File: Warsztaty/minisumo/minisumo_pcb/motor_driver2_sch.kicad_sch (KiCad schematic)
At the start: 6 parts, among them U2 TB6612FNG

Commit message: chyba gotowy schemat
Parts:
- removed C3, C6: 10nF, Capacitor_SMD:C_0805_2012Metric_Pad1.18x1.45mm_HandSolder, symbol Device:C_Small
- removed C4, C5: 10uF, Capacitor_Tantalum_SMD:CP_EIA-3528-12_Kemet-T, symbol Device:C_Polarized_Small
- removed M1: ~, Motors_KoNaR:KoNaR_Motor, symbol Motors_KoNaR:Motor
- removed U2: TB6612FNG, Package_SO:SSOP-24_5.3x8.2mm_P0.65mm, symbol Driver_Motor:TB6612FNG
- added C27, C30: 10uF, Capacitor_SMD:C_0805_2012Metric_Pad1.18x1.45mm_HandSolder, symbol Device:C_Polarized_Small
- added C28, C29: 10nF, Capacitor_SMD:C_0805_2012Metric_Pad1.18x1.45mm_HandSolder, symbol Device:C_Small
- added M2: ~, Motors_KoNaR:KoNaR_Motor, symbol Motors_KoNaR:Motor
- added U14: TB6612FNG, Package_SO:SSOP-24_5.3x8.2mm_P0.65mm, symbol Driver_Motor:TB6612FNG
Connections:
- net +5V: now also C27.1, C28.1, U14.19 (STBY), U14.20 (VCC)
- net +BATT: now also C29.1, C30.1, U14.13 (VM2), U14.14 (VM3), U14.24 (VM1)
- net GND: now also C27.2, C28.2, C29.2, C30.2, U14.10 (PGND2), U14.18 (GND), U14.3 (PGND1), U14.4 (PGND1), U14.9 (PGND2)
- new net: M2.1, U14.5 (AO2), U14.6 (AO2), U14.7 (BO2), U14.8 (BO2)
- new net: M2.2, U14.1 (AO1), U14.11 (BO1), U14.12 (BO1), U14.2 (AO1)
- new net DIRA_2: U14.17 (BIN1), U14.21 (AIN1)
- new net DIRB_2: U14.16 (BIN2), U14.22 (AIN2)
- new net PWM2: U14.15 (PWMB), U14.23 (PWMA)
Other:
- note added: "Motor 2 driver"
- note removed: "Motor 1 driver"

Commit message: stan przed usunięciem jednego czujnika lini
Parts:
- C27, C30: footprint Capacitor_SMD:C_0805_2012Metric_Pad1.18x1.45mm_HandSolder -> Capacitor_Tantalum_SMD:CP_EIA-3528-12_Kemet-T
- C28, C29: footprint Capacitor_SMD:C_0805_2012Metric_Pad1.18x1.45mm_HandSolder -> Capacitor_SMD:C_0805_2012Metric
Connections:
- net MOTOR_IN2: now reaches M2.1, U14.5 (AO2), U14.6 (AO2), U14.7 (BO2), U14.8 (BO2)
- net MOTOR_IN1: now reaches M2.2, U14.1 (AO1), U14.11 (BO1), U14.12 (BO1), U14.2 (AO1)
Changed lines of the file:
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@@
+		)
+	)
+	(label "MOTOR_IN2"
+		(at 76.2 55.88 0)
+		(fields_autoplaced yes)
+		(effects
+			(font
+				(size 1.27 1.27)
+			)
+			(justify left bottom)
+		)
+	)
+	(label "MOTOR_IN1"
+		(at 76.2 45.72 0)
+		(fields_autoplaced yes)
+		(effects
+			(font
+				(size 1.27 1.27)
+			)
+			(justify left bottom)
 		)
 	)
@@
 			)
 		)
-		(property "Footprint" "Capacitor_SMD:C_0805_2012Metric_Pad1.18x1.45mm_HandSolder"
+		(property "Footprint" "Capacitor_SMD:C_0805_2012Metric"
 			(at 72.39 29.21 0)
 			(effects
@@
 			)
 		)
-		(property "Footprint" "Capacitor_SMD:C_0805_2012Metric_Pad1.18x1.45mm_HandSolder"
+		(property "Footprint" "Capacitor_Tantalum_SMD:CP_EIA-3528-12_Kemet-T"
 			(at 77.47 29.21 0)
 			(effects
@@
 			)
 		)
-		(property "Footprint" "Capacitor_SMD:C_0805_2012Metric_Pad1.18x1.45mm_HandSolder"
+		(property "Footprint" "Capacitor_SMD:C_0805_2012Metric"
 			(at 31.75 30.48 0)
 			(effects
@@
 			)
 		)
-		(property "Footprint" "Capacitor_SMD:C_0805_2012Metric_Pad1.18x1.45mm_HandSolder"
+		(property "Footprint" "Capacitor_Tantalum_SMD:CP_EIA-3528-12_Kemet-T"
 			(at 26.67 30.48 0)
 			(effects

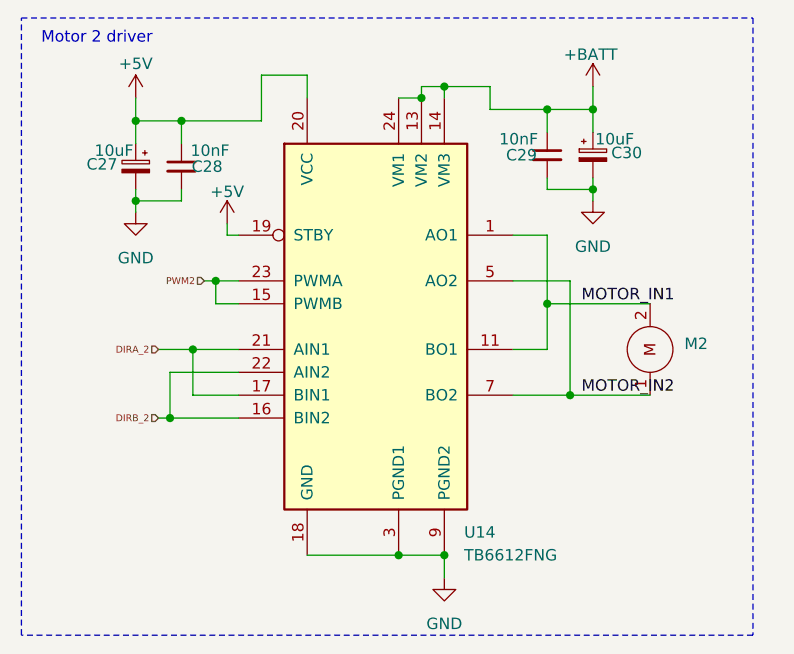
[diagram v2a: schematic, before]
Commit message: Wstępny wyglad robota i płytki
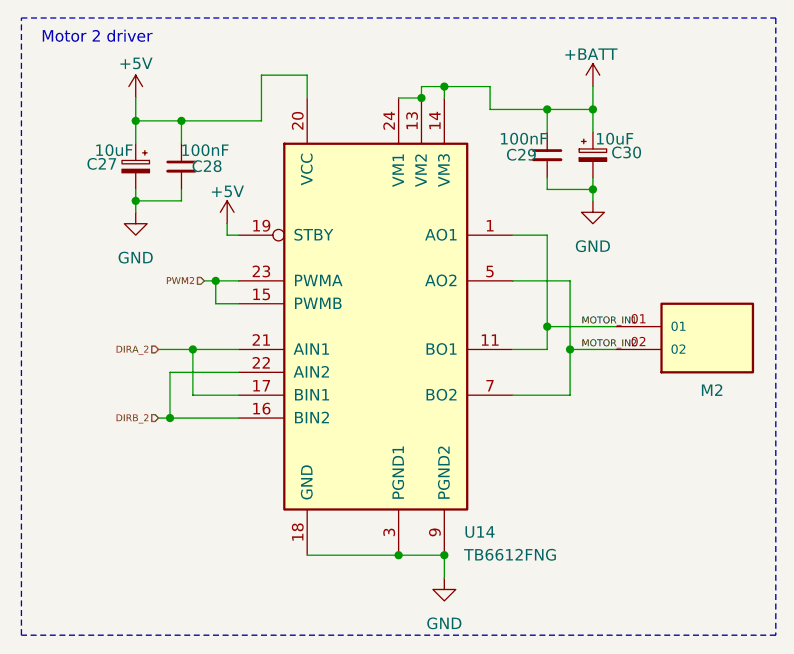
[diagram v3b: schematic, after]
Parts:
- removed M2: ~, Motors_KoNaR:KoNaR_Motor, symbol Motors_KoNaR:Motor
- added M2: HTSW-102-08-L-S, HTSW-102-08-L-S:SAMTEC_HTSW-102-08-L-S, symbol HTSW-102-08-L-S:HTSW-102-08-L-S
- C28, C29: value 10nF -> 100nF
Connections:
- net MOTOR_IN1: now also M2.01
- net MOTOR_IN2: now also M2.02
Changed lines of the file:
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@@
+	)
+	(junction
+		(at 74.93 50.8)
+		(diameter 0)
+		(color 0 0 0 0)
+	)
+	(junction
+		(at 72.39 48.26)
+		(diameter 0)
+		(color 0 0 0 0)
 	)
 	(junction
@@
 	)
 	(junction
-		(at 74.93 55.88)
-		(diameter 0)
-		(color 0 0 0 0)
-	)
-	(junction
 		(at 26.67 34.29)
-		(diameter 0)
-		(color 0 0 0 0)
-	)
-	(junction
-		(at 72.39 45.72)
 		(diameter 0)
 		(color 0 0 0 0)
@@
 	(wire
 		(pts
+			(xy 74.93 50.8) (xy 74.93 55.88)
+		)
+		(stroke
+			(width 0)
+			(type default)
+		)
+	)
+	(wire
+		(pts
 			(xy 31.75 25.4) (xy 40.64 25.4)
 		)
@@
 	(wire
 		(pts
-			(xy 72.39 45.72) (xy 72.39 50.8)
-		)
-		(stroke
-			(width 0)
-			(type default)
-		)
-	)
-	(wire
-		(pts
 			(xy 34.29 43.18) (xy 35.56 43.18)
 		)
@@
 	(wire
 		(pts
-			(xy 72.39 38.1) (xy 72.39 45.72)
-		)
-		(stroke
-			(width 0)
-			(type default)
-		)
-	)
-	(wire
-		(pts
-			(xy 74.93 55.88) (xy 83.82 55.88)
+			(xy 72.39 38.1) (xy 72.39 48.26)
 		)
 		(stroke
@@
 	(wire
 		(pts
+			(xy 72.39 48.26) (xy 80.01 48.26)
+		)
+		(stroke
+			(width 0)
+			(type default)
+		)
+	)
+	(wire
+		(pts
 			(xy 30.48 58.42) (xy 38.1 58.42)
 		)
@@
 	(wire
 		(pts
-			(xy 74.93 43.18) (xy 74.93 55.88)
+			(xy 74.93 43.18) (xy 74.93 50.8)
 		)
 		(stroke
@@
 	(wire
 		(pts
+			(xy 72.39 48.26) (xy 72.39 50.8)
+		)
+		(stroke
+			(width 0)
+			(type default)
+		)
+	)
+	(wire
+		(pts
 			(xy 40.64 20.32) (xy 40.64 25.4)
 		)
@@
 	(wire
 		(pts
+			(xy 74.93 50.8) (xy 80.01 50.8)
+		)
+		(stroke
+			(width 0)
+			(type default)
+		)
+	)
+	(wire
+		(pts
 			(xy 36.83 36.83) (xy 36.83 38.1)
 		)
@@
 		(pts
 			(xy 66.04 24.13) (xy 66.04 21.59)
-		)
-		(stroke
-			(width 0)
-			(type default)
-		)
-	)
-	(wire
-		(pts
-			(xy 72.39 45.72) (xy 83.82 45.72)
 		)
 		(stroke
@@
 	(rectangle
 		(start 13.97 13.97)
-		(end 95.25 82.55)
+		(end 97.79 82.55)
 		(stroke
 			(width 0)
@@
 	)
 	(label "MOTOR_IN2"
-		(at 76.2 55.88 0)
+		(at 76.2 50.8 0)
 		(fields_autoplaced yes)
 		(effects
 			(font
-				(size 1.27 1.27)
+				(size 0.762 0.762)
 			)
 			(justify left bottom)
@@
 	)
 	(label "MOTOR_IN1"
-		(at 76.2 45.72 0)
+		(at 76.2 48.26 0)
 		(fields_autoplaced yes)
 		(effects
 			(font
-				(size 1.27 1.27)
+				(size 0.762 0.762)
 			)
 			(justify left bottom)
@@
 			)
 		)
-		(property "Value" "10nF"
+		(property "Value" "100nF"
 			(at 67.056 27.432 0)
 			(effects
@@
 	)
 	(symbol
+		(lib_id "HTSW-102-08-L-S:HTSW-102-08-L-S")
+		(at 90.17 48.26 0)
+		(unit 1)
+		(exclude_from_sim no)
+		(in_bom yes)
+		(on_board yes)
+		(dnp no)
+		(property "Reference" "M2"
+			(at 89.408 55.372 0)
+			(effects
+				(font
+					(size 1.27 1.27)
+				)
+				(justify left)
+			)
+		)
+		(property "Value" "HTSW-102-08-L-S"
+			(at 76.962 43.434 0)
+			(effects
+				(font
+					(size 1.27 1.27)
+				)
+				(justify left)
+				(hide yes)
+			)
+		)
+		(property "Footprint" "HTSW-102-08-L-S:SAMTEC_HTSW-102-08-L-S"
+			(at 90.17 48.26 0)
+			(effects
+				(font
+					(size 1.27 1.27)
+				)
+				(justify bottom)
+				(hide yes)
+			)
+		)
+		(property "Datasheet" ""
+			(at 90.17 48.26 0)
+			(effects
+				(font
+					(size 1.27 1.27)
+				)
+				(hide yes)
+			)
+		)
+		(property "Description" ""
+			(at 90.17 48.26 0)
+			(effects
+				(font
+					(size 1.27 1.27)
+				)
+				(hide yes)
+			)
+		)
+		(property "MF" "Samtec Inc."
+			(at 90.17 48.26 0)
+			(effects
+				(font
+					(size 1.27 1.27)
+				)
+				(justify bottom)
+				(hide yes)
+			)
+		)
+		(property "Description_1" "\nConn Unshrouded Header HDR 2 POS 2.54mm Solder ST Top Entry Thru-Hole Bag\n"
+			(at 90.17 48.26 0)
+			(effects
+				(font
+					(size 1.27 1.27)
+				)
+				(justify bottom)
+				(hide yes)
+			)
+		)
+		(property "Package" "None"
+			(at 90.17 48.26 0)
+			(effects
+				(font
+					(size 1.27 1.27)
+				)
+				(justify bottom)
+				(hide yes)
+			)
+		)
+		(property "Price" "None"
+			(at 90.17 48.26 0)
+			(effects
+				(font
+					(size 1.27 1.27)
+				)
+				(justify bottom)
+				(hide yes)
+			)
+		)
+		(property "Check_prices" "https://www.snapeda.com/parts/HTSW-102-08-L-S/Samtec/view-part/?ref=eda"
+			(at 90.17 48.26 0)
+			(effects
+				(font
+					(size 1.27 1.27)
+				)
+				(justify bottom)
+				(hide yes)
+			)
+		)
+		(property "SnapEDA_Link" "https://www.snapeda.com/parts/HTSW-102-08-L-S/Samtec/view-part/?ref=snap"
+			(at 90.17 48.26 0)
+			(effects
+				(font
+					(size 1.27 1.27)
+				)
+				(justify bottom)
+				(hide yes)
+			)
+		)
+		(property "MP" "HTSW-102-08-L-S"
+			(at 90.17 48.26 0)
+			(effects
+				(font
+					(size 1.27 1.27)
+				)
+				(justify bottom)
+				(hide yes)
+			)
+		)
+		(property "Availability" "In Stock"
+			(at 90.17 48.26 0)
+			(effects
+				(font
+					(size 1.27 1.27)
+				)
+				(justify bottom)
+				(hide yes)
+			)
+		)
+		(property "Purchase-URL" "https://pricing.snapeda.com/search/part/HTSW-102-25-G-S/?ref=eda"
+			(at 90.17 48.26 0)
+			(effects
+				(font
+					(size 1.27 1.27)
+				)
+				(justify bottom)
+				(hide yes)
+			)
+		)
+		(pin "02"
+		)
+		(pin "01"
+		)
+		(instances
+			(project "minisumo_pcb"
+				(path "/7b99a4ad-c15f-48f5-acdf-b2b295c8ee3b/da52437e-b83d-4b13-8d2c-d0930bef3ed5"
+					(reference "M2")
+					(unit 1)
+				)
+			)
+		)
+	)
+	(symbol
 		(lib_id "power:+BATT")
 		(at 77.47 21.59 0)
@@
 			)
 		)
-		(property "Value" "10nF"
+		(property "Value" "100nF"
 			(at 37.084 28.702 0)
 			(effects
@@
 					(unit 1)
 				)
-			)
-		)
-	)
-	(symbol
-		(lib_id "Motors_KoNaR:Motor")
-		(at 83.82 50.8 90)
-		(unit 1)
-		(exclude_from_sim no)
-		(in_bom yes)
-		(on_board yes)
-		(dnp no)
-		(fields_autoplaced yes)
-		(property "Reference" "M2"
-			(at 87.63 50.1649 90)
-			(effects
-				(font
-					(size 1.27 1.27)
-				)
-				(justify right)
-			)
-		)
-		(property "Value" "~"
-			(at 87.63 52.07 90)
-			(effects
-				(font
-					(size 1.27 1.27)
-				)
-				(justify right)
-			)
-		)
-		(property "Footprint" "Motors_KoNaR:KoNaR_Motor"
-			(at 87.884 50.8 0)
-			(effects
-				(font
-					(size 1.27 1.27)
-				)
-				(hide yes)
-			)
-		)
-		(property "Datasheet" ""
-			(at 83.82 50.8 0)
-			(effects
-				(font
-					(size 1.27 1.27)
-				)
-				(hide yes)
-			)
-		)
-		(property "Description" ""
-			(at 83.82 50.8 0)
-			(effects
-				(font
-					(size 1.27 1.27)
-				)
-				(hide yes)
-			)
-		)
-		(pin "1"
-		)
-		(pin "2"
-		)
-		(instances
-			(project "minisumo_pcb"
-				(path "/7b99a4ad-c15f-48f5-acdf-b2b295c8ee3b/da52437e-b83d-4b13-8d2c-d0930bef3ed5"
-					(reference "M2")
-					(unit 1)
-				)

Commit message: koncowy projekt plytki i chyba model tez
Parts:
- renumbered U14 to M_DRIVER2
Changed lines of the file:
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@@
 		(dnp no)
 		(fields_autoplaced yes)
-		(property "Reference" "U14"
+		(property "Reference" "M_DRIVER2"
 			(at 63.1541 71.12 0)
 			(effects
@@
 			(project "minisumo_pcb"
 				(path "/7b99a4ad-c15f-48f5-acdf-b2b295c8ee3b/da52437e-b83d-4b13-8d2c-d0930bef3ed5"
-					(reference "U14")
+					(reference "M_DRIVER2")
 					(unit 1)
 				)
